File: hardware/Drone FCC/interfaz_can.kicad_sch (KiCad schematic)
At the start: 14 parts, among them J801 CAN 1 Connector 1, J803 CAN 2 Connector 1, U801 SN65HVD230, U802 SN65HVD230

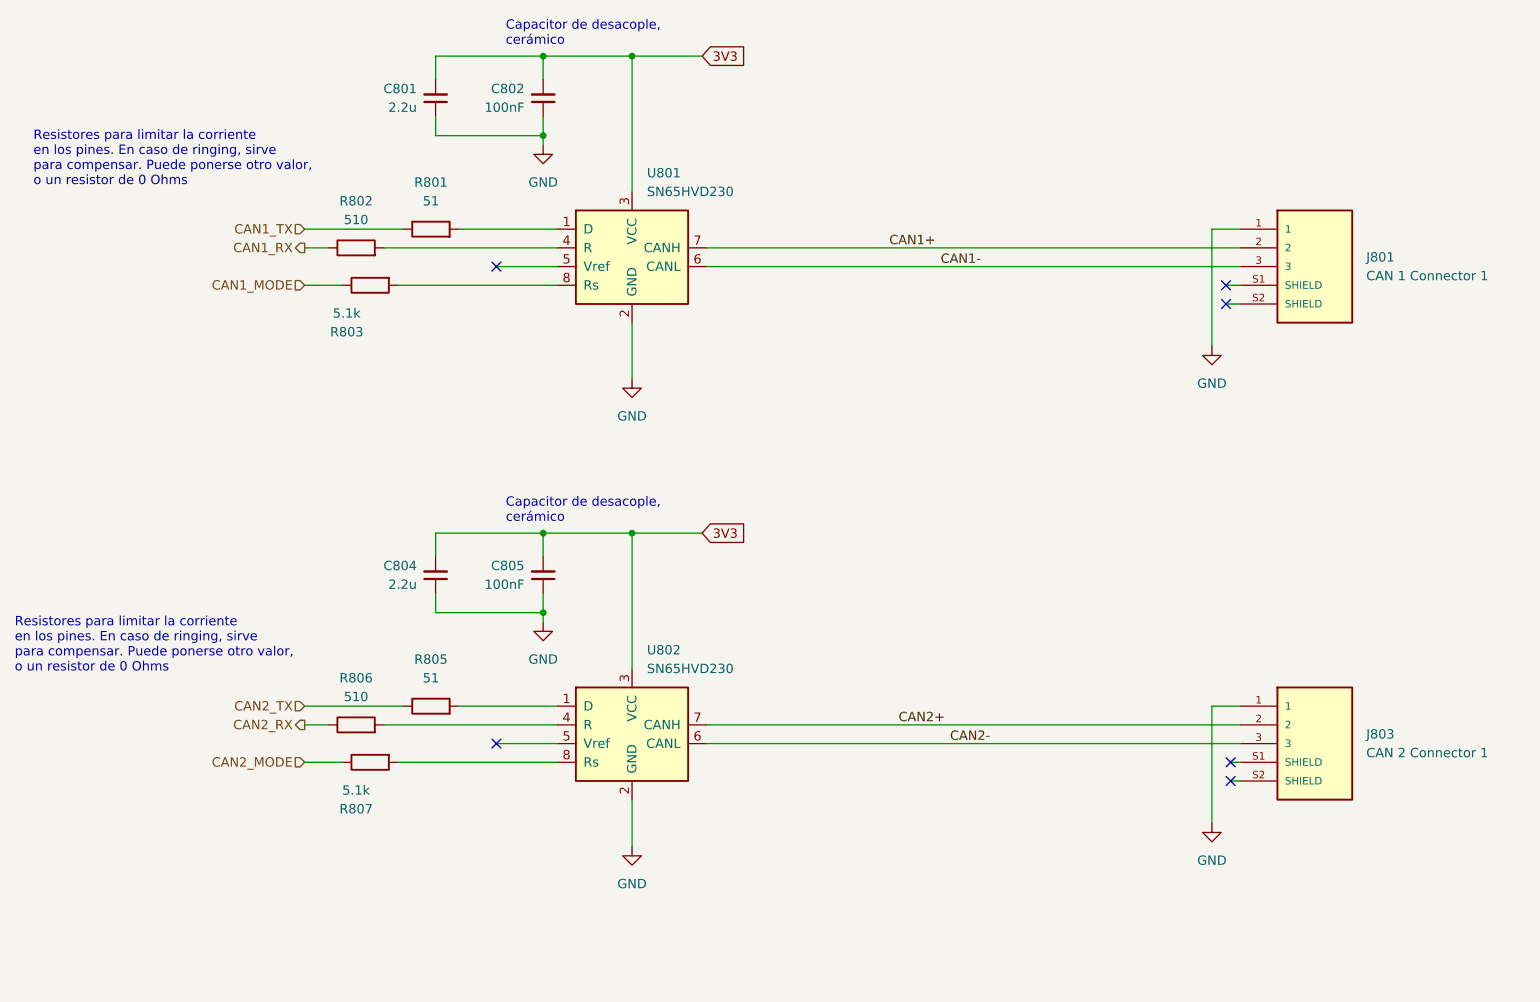
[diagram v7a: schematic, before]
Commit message: tidying up the schematic
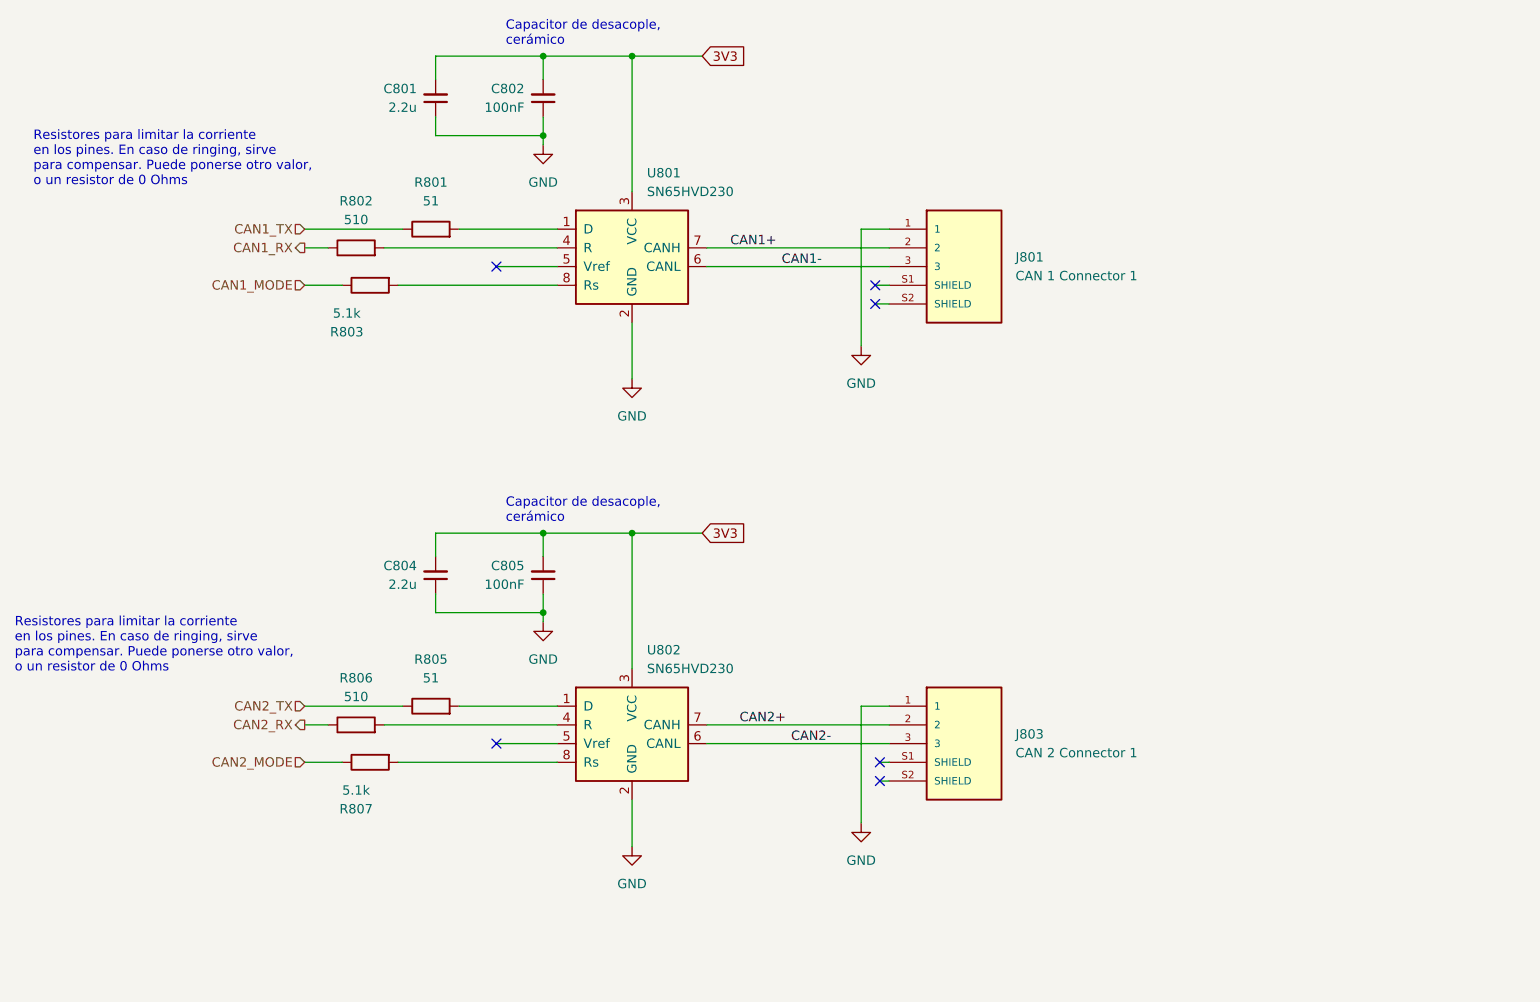
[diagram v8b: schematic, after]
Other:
- moved on the sheet: J801, J803
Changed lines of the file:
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@@
   (junction (at 133.35 36.83) (diameter 0) (color 0 0 0 0)
   )
-  (no_connect (at 226.06 57.15))
-  (no_connect (at 226.695 121.92))
-  (no_connect (at 226.06 59.69))
-  (no_connect (at 226.695 124.46))
+  (no_connect (at 178.435 57.15))
+  (no_connect (at 179.07 121.92))
+  (no_connect (at 178.435 59.69))
+  (no_connect (at 179.07 124.46))
   (no_connect (at 127 54.61))
   (no_connect (at 127 119.38))
@@
     (stroke (width 0) (type default) (color 0 0 0 0))
   )
-  (wire (pts (xy 226.695 124.46) (xy 227.965 124.46))
+  (wire (pts (xy 179.07 124.46) (xy 180.34 124.46))
     (stroke (width 0) (type default) (color 0 0 0 0))
   )
@@
     (stroke (width 0) (type default) (color 0 0 0 0))
   )
-  (wire (pts (xy 155.575 116.84) (xy 227.965 116.84))
-    (stroke (width 0) (type default) (color 0 0 0 0))
-  )
-  (wire (pts (xy 226.06 57.15) (xy 227.965 57.15))
+  (wire (pts (xy 178.435 57.15) (xy 180.34 57.15))
     (stroke (width 0) (type default) (color 0 0 0 0))
   )
@@
     (stroke (width 0) (type default) (color 0 0 0 0))
   )
-  (wire (pts (xy 155.575 52.07) (xy 227.965 52.07))
-    (stroke (width 0) (type default) (color 0 0 0 0))
-  )
   (wire (pts (xy 145.415 62.23) (xy 145.415 69.85))
     (stroke (width 0) (type default) (color 0 0 0 0))
   )
-  (wire (pts (xy 224.155 49.53) (xy 224.155 65.405))
+  (wire (pts (xy 176.53 49.53) (xy 176.53 65.405))
     (stroke (width 0) (type default) (color 0 0 0 0))
   )
@@
     (stroke (width 0) (type default) (color 0 0 0 0))
   )
-  (wire (pts (xy 224.155 114.3) (xy 224.155 130.175))
+  (wire (pts (xy 155.575 116.84) (xy 180.34 116.84))
+    (stroke (width 0) (type default) (color 0 0 0 0))
+  )
+  (wire (pts (xy 155.575 54.61) (xy 180.34 54.61))
+    (stroke (width 0) (type default) (color 0 0 0 0))
+  )
+  (wire (pts (xy 155.575 52.07) (xy 180.34 52.07))
+    (stroke (width 0) (type default) (color 0 0 0 0))
+  )
+  (wire (pts (xy 176.53 114.3) (xy 176.53 130.175))
     (stroke (width 0) (type default) (color 0 0 0 0))
   )
@@
     (stroke (width 0) (type default) (color 0 0 0 0))
   )
-  (wire (pts (xy 226.06 59.69) (xy 227.965 59.69))
+  (wire (pts (xy 178.435 59.69) (xy 180.34 59.69))
     (stroke (width 0) (type default) (color 0 0 0 0))
   )
@@
     (stroke (width 0) (type default) (color 0 0 0 0))
   )
-  (wire (pts (xy 155.575 119.38) (xy 227.965 119.38))
-    (stroke (width 0) (type default) (color 0 0 0 0))
-  )
   (wire (pts (xy 133.35 90.805) (xy 133.35 93.98))
     (stroke (width 0) (type default) (color 0 0 0 0))
@@
     (stroke (width 0) (type default) (color 0 0 0 0))
   )
+  (wire (pts (xy 155.575 119.38) (xy 180.34 119.38))
+    (stroke (width 0) (type default) (color 0 0 0 0))
+  )
   (wire (pts (xy 133.35 34.29) (xy 133.35 36.83))
     (stroke (width 0) (type default) (color 0 0 0 0))
@@
     (stroke (width 0) (type default) (color 0 0 0 0))
   )
-  (wire (pts (xy 155.575 54.61) (xy 227.965 54.61))
-    (stroke (width 0) (type default) (color 0 0 0 0))
-  )
   (wire (pts (xy 145.415 127) (xy 145.415 133.35))
     (stroke (width 0) (type default) (color 0 0 0 0))
@@
     (stroke (width 0) (type default) (color 0 0 0 0))
   )
-  (wire (pts (xy 224.155 114.3) (xy 227.965 114.3))
+  (wire (pts (xy 176.53 114.3) (xy 180.34 114.3))
     (stroke (width 0) (type default) (color 0 0 0 0))
   )
@@
     (stroke (width 0) (type default) (color 0 0 0 0))
   )
-  (wire (pts (xy 226.695 121.92) (xy 227.965 121.92))
+  (wire (pts (xy 179.07 121.92) (xy 180.34 121.92))
     (stroke (width 0) (type default) (color 0 0 0 0))
   )
@@
     (stroke (width 0) (type default) (color 0 0 0 0))
   )
-  (wire (pts (xy 227.965 49.53) (xy 224.155 49.53))
+  (wire (pts (xy 180.34 49.53) (xy 176.53 49.53))
     (stroke (width 0) (type default) (color 0 0 0 0))
   )
@@
     (effects (font (size 1.27 1.27)) (justify left bottom))
   )
-  (label "CAN2+" (at 181.61 116.84 0)
-    (effects (font (size 1.27 1.27)) (justify left bottom))
-  )
-  (label "CAN2-" (at 188.595 119.38 0)
-    (effects (font (size 1.27 1.27)) (justify left bottom))
-  )
-  (label "CAN1-" (at 187.325 54.61 0)
-    (effects (font (size 1.27 1.27)) (justify left bottom))
-  )
-  (label "CAN1+" (at 180.34 52.07 0)
+  (label "CAN2+" (at 160.02 116.84 0)
+    (effects (font (size 1.27 1.27)) (justify left bottom))
+  )
+  (label "CAN2-" (at 167.005 119.38 0)
+    (effects (font (size 1.27 1.27)) (justify left bottom))
+  )
+  (label "CAN1-" (at 165.735 54.61 0)
+    (effects (font (size 1.27 1.27)) (justify left bottom))
+  )
+  (label "CAN1+" (at 158.75 52.07 0)
     (effects (font (size 1.27 1.27)) (justify left bottom))
   )
@@
     (pin "8")
   )
-  (symbol (lib_name "GND_2") (lib_id "power:GND") (at 224.155 130.175 0) (unit 1)
-    (in_bom yes) (on_board yes) (fields_autoplaced)
-    (property "Reference" "#PWR0104" (id 0) (at 224.155 136.525 0)
-      (effects (font (size 1.27 1.27)) hide)
-    )
-    (property "Value" "GND" (id 1) (at 224.155 135.255 0))
-    (property "Footprint" "" (id 2) (at 224.155 130.175 0)
-      (effects (font (size 1.27 1.27)) hide)
-    )
-    (property "Datasheet" "" (id 3) (at 224.155 130.175 0)
-      (effects (font (size 1.27 1.27)) hide)
-    )
-    (pin "1")
-  )
-  (symbol (lib_id "DF13A-3P-1.25H(21):HRS_DF13A-3P-1.25H(21)") (at 236.855 137.16 0) (unit 1)
-    (in_bom yes) (on_board yes) (fields_autoplaced)
-    (property "Reference" "J803" (id 0) (at 245.11 118.1099 0)
-      (effects (font (size 1.27 1.27)) (justify left))
-    )
-    (property "Value" "CAN 2 Connector 1" (id 1) (at 245.11 120.6499 0)
-      (effects (font (size 1.27 1.27)) (justify left))
-    )
-    (property "Footprint" "DF13A-3P-1.25H(21):HRS_DF13A-3P-1.25H(21)" (id 2) (at 244.475 132.08 0)
+  (symbol (lib_name "GND_2") (lib_id "power:GND") (at 176.53 130.175 0) (unit 1)
+    (in_bom yes) (on_board yes) (fields_autoplaced)
+    (property "Reference" "#PWR0104" (id 0) (at 176.53 136.525 0)
+      (effects (font (size 1.27 1.27)) hide)
+    )
+    (property "Value" "GND" (id 1) (at 176.53 135.255 0))
+    (property "Footprint" "" (id 2) (at 176.53 130.175 0)
+      (effects (font (size 1.27 1.27)) hide)
+    )
+    (property "Datasheet" "" (id 3) (at 176.53 130.175 0)
+      (effects (font (size 1.27 1.27)) hide)
+    )
+    (pin "1")
+  )
+  (symbol (lib_id "DF13A-3P-1.25H(21):HRS_DF13A-3P-1.25H(21)") (at 189.23 137.16 0) (unit 1)
+    (in_bom yes) (on_board yes) (fields_autoplaced)
+    (property "Reference" "J803" (id 0) (at 197.485 118.1099 0)
+      (effects (font (size 1.27 1.27)) (justify left))
+    )
+    (property "Value" "CAN 2 Connector 1" (id 1) (at 197.485 120.6499 0)
+      (effects (font (size 1.27 1.27)) (justify left))
+    )
+    (property "Footprint" "DF13A-3P-1.25H(21):HRS_DF13A-3P-1.25H(21)" (id 2) (at 196.85 132.08 0)
       (effects (font (size 1.27 1.27)) (justify bottom) hide)
     )
-    (property "Datasheet" "" (id 3) (at 236.855 130.81 0)
-      (effects (font (size 1.27 1.27)) hide)
-    )
-    (property "MANUFACTURER" "HRS" (id 4) (at 236.855 130.81 0)
+    (property "Datasheet" "" (id 3) (at 189.23 130.81 0)
+      (effects (font (size 1.27 1.27)) hide)
+    )
+    (property "MANUFACTURER" "HRS" (id 4) (at 189.23 130.81 0)
       (effects (font (size 1.27 1.27)) (justify bottom) hide)
     )
@@
     (pin "2")
   )
-  (symbol (lib_name "GND_2") (lib_id "power:GND") (at 224.155 65.405 0) (unit 1)
-    (in_bom yes) (on_board yes) (fields_autoplaced)
-    (property "Reference" "#PWR0101" (id 0) (at 224.155 71.755 0)
-      (effects (font (size 1.27 1.27)) hide)
-    )
-    (property "Value" "GND" (id 1) (at 224.155 70.485 0))
-    (property "Footprint" "" (id 2) (at 224.155 65.405 0)
-      (effects (font (size 1.27 1.27)) hide)
-    )
-    (property "Datasheet" "" (id 3) (at 224.155 65.405 0)
-      (effects (font (size 1.27 1.27)) hide)
-    )
-    (pin "1")
-  )
-  (symbol (lib_id "DF13A-3P-1.25H(21):HRS_DF13A-3P-1.25H(21)") (at 236.855 72.39 0) (unit 1)
-    (in_bom yes) (on_board yes) (fields_autoplaced)
-    (property "Reference" "J801" (id 0) (at 245.11 53.3399 0)
-      (effects (font (size 1.27 1.27)) (justify left))
-    )
-    (property "Value" "CAN 1 Connector 1" (id 1) (at 245.11 55.8799 0)
-      (effects (font (size 1.27 1.27)) (justify left))
-    )
-    (property "Footprint" "DF13A-3P-1.25H(21):HRS_DF13A-3P-1.25H(21)" (id 2) (at 244.475 67.31 0)
+  (symbol (lib_name "GND_2") (lib_id "power:GND") (at 176.53 65.405 0) (unit 1)
+    (in_bom yes) (on_board yes) (fields_autoplaced)
+    (property "Reference" "#PWR0101" (id 0) (at 176.53 71.755 0)
+      (effects (font (size 1.27 1.27)) hide)
+    )
+    (property "Value" "GND" (id 1) (at 176.53 70.485 0))
+    (property "Footprint" "" (id 2) (at 176.53 65.405 0)
+      (effects (font (size 1.27 1.27)) hide)
+    )
+    (property "Datasheet" "" (id 3) (at 176.53 65.405 0)
+      (effects (font (size 1.27 1.27)) hide)
+    )
+    (pin "1")
+  )
+  (symbol (lib_id "DF13A-3P-1.25H(21):HRS_DF13A-3P-1.25H(21)") (at 189.23 72.39 0) (unit 1)
+    (in_bom yes) (on_board yes) (fields_autoplaced)
+    (property "Reference" "J801" (id 0) (at 197.485 53.3399 0)
+      (effects (font (size 1.27 1.27)) (justify left))
+    )
+    (property "Value" "CAN 1 Connector 1" (id 1) (at 197.485 55.8799 0)
+      (effects (font (size 1.27 1.27)) (justify left))
+    )
+    (property "Footprint" "DF13A-3P-1.25H(21):HRS_DF13A-3P-1.25H(21)" (id 2) (at 196.85 67.31 0)
       (effects (font (size 1.27 1.27)) (justify bottom) hide)
     )
-    (property "Datasheet" "" (id 3) (at 236.855 66.04 0)
-      (effects (font (size 1.27 1.27)) hide)
-    )
-    (property "MANUFACTURER" "HRS" (id 4) (at 236.855 66.04 0)
+    (property "Datasheet" "" (id 3) (at 189.23 66.04 0)
+      (effects (font (size 1.27 1.27)) hide)
+    )
+    (property "MANUFACTURER" "HRS" (id 4) (at 189.23 66.04 0)
       (effects (font (size 1.27 1.27)) (justify bottom) hide)
     )
